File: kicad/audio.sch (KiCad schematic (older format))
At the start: 20 parts

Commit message: ...
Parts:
- added J303: ST-214N, symbol JACK_TRS_6PINS
- gave numbers to parts that had none: 17
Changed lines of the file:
@@
 LIBS:contrib
 LIBS:valves
+LIBS:stm32
 LIBS:ad1955
-LIBS:dcdc
-LIBS:transformer
-LIBS:ir4427
-LIBS:irf9956
-LIBS:usblc6-2
+LIBS:lm4864
 LIBS:synth-cache
 EELAYER 25 0
@@
 $EndDescr
 $Comp
-L JACK_TRS_6PINS J?
+L JACK_TRS_6PINS J301
 U 1 1 5677AE4D
 P 1650 2500
-F 0 "J?" H 1650 2900 50  0000 C CNN
+F 0 "J301" H 1650 2900 50  0000 C CNN
 F 1 "ST-214N" H 1600 2200 50  0000 C CNN
 F 2 "" H 1750 2350 50  0000 C CNN
@@
 $EndComp
 $Comp
-L JACK_TRS_6PINS J?
+L JACK_TRS_6PINS J302
 U 1 1 5677AEE6
 P 1650 4850
-F 0 "J?" H 1650 5250 50  0000 C CNN
+F 0 "J302" H 1650 5250 50  0000 C CNN
 F 1 "ST-214N" H 1600 4550 50  0000 C CNN
 F 2 "" H 1750 4700 50  0000 C CNN
@@
 $EndComp
 $Comp
-L MCP6004 U?
+L MCP6004 U301
 U 1 1 5677B105
 P 3750 1800
-F 0 "U?" H 3800 2000 50  0000 C CNN
+F 0 "U301" H 3800 2000 50  0000 C CNN
 F 1 "AD824" H 3900 1600 50  0000 C CNN
 F 2 "" H 3700 1900 50  0000 C CNN
@@
 $EndComp
 $Comp
-L MCP6004 U?
+L MCP6004 U301
 U 2 1 5677B146
 P 3750 2950
-F 0 "U?" H 3800 3150 50  0000 C CNN
+F 0 "U301" H 3800 3150 50  0000 C CNN
 F 1 "AD824" H 3900 2750 50  0000 C CNN
 F 2 "" H 3700 3050 50  0000 C CNN
@@
 $EndComp
 $Comp
-L MCP6004 U?
+L MCP6004 U301
 U 3 1 5677B1C5
 P 3750 4150
-F 0 "U?" H 3800 4350 50  0000 C CNN
+F 0 "U301" H 3800 4350 50  0000 C CNN
 F 1 "AD824" H 3900 3950 50  0000 C CNN
 F 2 "" H 3700 4250 50  0000 C CNN
@@
 $EndComp
 $Comp
-L MCP6004 U?
+L MCP6004 U301
 U 4 1 5677B248
 P 3750 5350
-F 0 "U?" H 3800 5550 50  0000 C CNN
+F 0 "U301" H 3800 5550 50  0000 C CNN
 F 1 "AD824" H 3900 5150 50  0000 C CNN
 F 2 "" H 3700 5450 50  0000 C CNN
@@
 $EndComp
 $Comp
-L CP1 C?
+L CP1 C301
 U 1 1 5677B391
 P 2700 1900
-F 0 "C?" H 2725 2000 50  0000 L CNN
+F 0 "C301" H 2725 2000 50  0000 L CNN
 F 1 "10.0" H 2725 1800 50  0000 L CNN
 F 2 "" H 2700 1900 50  0000 C CNN
@@
 $EndComp
 $Comp
-L R_Small R?
+L R_Small R301
 U 1 1 5677B458
 P 3150 1900
-F 0 "R?" H 3180 1920 50  0000 L CNN
+F 0 "R301" H 3180 1920 50  0000 L CNN
 F 1 "1K" H 3180 1860 50  0000 L CNN
 F 2 "" H 3150 1900 50  0000 C CNN
@@
 	2350 1900 2550 1900
 $Comp
-L R_Small R?
+L R_Small R308
 U 1 1 5677B594
 P 3850 1200
-F 0 "R?" H 3900 1250 50  0000 L CNN
+F 0 "R308" H 3900 1250 50  0000 L CNN
 F 1 "100K" H 3900 1150 50  0000 L CNN
 F 2 "" H 3850 1200 50  0000 C CNN
@@
 Connection ~ 4050 1800
 $Comp
-L GNDA #PWR?
+L GNDA #PWR046
 U 1 1 5677B8F7
 P 3650 2100
-F 0 "#PWR?" H 3650 1850 50  0001 C CNN
+F 0 "#PWR046" H 3650 1850 50  0001 C CNN
 F 1 "GNDA" H 3650 1950 39  0000 C CNN
 F 2 "" H 3650 2100 50  0000 C CNN
@@
 $EndComp
 Wire Wire Line
-	3650 900  3650 1000
-Wire Wire Line
-	3650 1000 3650 1500
+	3650 900  3650 1500
 Text Label 3650 900  0    60   ~ 0
 +3V3A_CPU
 $Comp
-L CP1 C?
+L CP1 C302
 U 1 1 5677BFEC
 P 2700 3050
-F 0 "C?" H 2725 3150 50  0000 L CNN
+F 0 "C302" H 2725 3150 50  0000 L CNN
 F 1 "10.0" H 2725 2950 50  0000 L CNN
 F 2 "" H 2700 3050 50  0000 C CNN
@@
 $EndComp
 $Comp
-L R_Small R?
+L R_Small R302
 U 1 1 5677BFF2
 P 3150 3050
-F 0 "R?" H 3180 3070 50  0000 L CNN
+F 0 "R302" H 3180 3070 50  0000 L CNN
 F 1 "1K" H 3180 3010 50  0000 L CNN
 F 2 "" H 3150 3050 50  0000 C CNN
@@
 	2350 3050 2550 3050
 $Comp
-L R_Small R?
+L R_Small R305
 U 1 1 5677BFFB
 P 3800 2550
-F 0 "R?" H 3850 2600 50  0000 L CNN
+F 0 "R305" H 3850 2600 50  0000 L CNN
 F 1 "100K" H 3850 2500 50  0000 L CNN
 F 2 "" H 3800 2550 50  0000 C CNN
@@
 Connection ~ 4050 2950
 $Comp
-L GNDA #PWR?
+L GNDA #PWR047
 U 1 1 5677C008
 P 3650 3250
-F 0 "#PWR?" H 3650 3000 50  0001 C CNN
+F 0 "#PWR047" H 3650 3000 50  0001 C CNN
 F 1 "GNDA" H 3650 3100 39  0000 C CNN
 F 2 "" H 3650 3250 50  0000 C CNN
@@
 $EndComp
 $Comp
-L CP1 C?
+L CP1 C303
 U 1 1 5677C595
 P 2700 4250
-F 0 "C?" H 2725 4350 50  0000 L CNN
+F 0 "C303" H 2725 4350 50  0000 L CNN
 F 1 "10.0" H 2725 4150 50  0000 L CNN
 F 2 "" H 2700 4250 50  0000 C CNN
@@
 $EndComp
 $Comp
-L R_Small R?
+L R_Small R303
 U 1 1 5677C59B
 P 3150 4250
-F 0 "R?" H 3180 4270 50  0000 L CNN
+F 0 "R303" H 3180 4270 50  0000 L CNN
 F 1 "1K" H 3180 4210 50  0000 L CNN
 F 2 "" H 3150 4250 50  0000 C CNN
@@
 	2550 4250 2400 4250
 $Comp
-L R_Small R?
+L R_Small R306
 U 1 1 5677C5A4
 P 3800 3750
-F 0 "R?" H 3850 3800 50  0000 L CNN
+F 0 "R306" H 3850 3800 50  0000 L CNN
 F 1 "100K" H 3850 3700 50  0000 L CNN
 F 2 "" H 3800 3750 50  0000 C CNN
@@
 Connection ~ 4050 4150
 $Comp
-L GNDA #PWR?
+L GNDA #PWR048
 U 1 1 5677C5B1
 P 3650 4450
-F 0 "#PWR?" H 3650 4200 50  0001 C CNN
+F 0 "#PWR048" H 3650 4200 50  0001 C CNN
 F 1 "GNDA" H 3650 4300 39  0000 C CNN
 F 2 "" H 3650 4450 50  0000 C CNN
@@
 $EndComp
 $Comp
-L CP1 C?
+L CP1 C304
 U 1 1 5677C832
 P 2700 5450
-F 0 "C?" H 2725 5550 50  0000 L CNN
+F 0 "C304" H 2725 5550 50  0000 L CNN
 F 1 "10.0" H 2725 5350 50  0000 L CNN
 F 2 "" H 2700 5450 50  0000 C CNN
@@
 $EndComp
 $Comp
-L R_Small R?
+L R_Small R304
 U 1 1 5677C838
 P 3150 5450
-F 0 "R?" H 3180 5470 50  0000 L CNN
+F 0 "R304" H 3180 5470 50  0000 L CNN
 F 1 "1K" H 3180 5410 50  0000 L CNN
 F 2 "" H 3150 5450 50  0000 C CNN
@@
 	2550 5450 2400 5450
 $Comp
-L R_Small R?
+L R_Small R307
 U 1 1 5677C841
 P 3800 4950
-F 0 "R?" H 3850 5000 50  0000 L CNN
+F 0 "R307" H 3850 5000 50  0000 L CNN
 F 1 "100K" H 3850 4900 50  0000 L CNN
 F 2 "" H 3800 4950 50  0000 C CNN
@@
 Connection ~ 4050 5350
 $Comp
-L GNDA #PWR?
+L GNDA #PWR049
 U 1 1 5677C84E
 P 3650 5650
-F 0 "#PWR?" H 3650 5400 50  0001 C CNN
+F 0 "#PWR049" H 3650 5400 50  0001 C CNN
 F 1 "GNDA" H 3650 5500 39  0000 C CNN
 F 2 "" H 3650 5650 50  0000 C CNN
@@
 $EndComp
 $Comp
-L CP1 C?
+L CP1 C305
 U 1 1 5677D086
 P 4750 1250
-F 0 "C?" H 4775 1350 50  0000 L CNN
+F 0 "C305" H 4775 1350 50  0000 L CNN
 F 1 "10.0" H 4775 1150 50  0000 L CNN
 F 2 "" H 4750 1250 50  0000 C CNN
@@
 $EndComp
 $Comp
-L C_Small C?
+L C_Small C306
 U 1 1 5677D24B
 P 5050 1250
-F 0 "C?" H 5060 1320 50  0000 L CNN
+F 0 "C306" H 5060 1320 50  0000 L CNN
 F 1 "C_Small" H 5060 1170 50  0000 L CNN
 F 2 "" H 5050 1250 50  0000 C CNN
@@
 $EndComp
 Wire Wire Line
-	4750 1100 4900 1100
-Wire Wire Line
-	4900 1100 5050 1100
+	4750 1100 5050 1100
 Wire Wire Line
 	5050 1100 5050 1150
 Wire Wire Line
-	4750 1400 4900 1400
-Wire Wire Line
-	4900 1400 5050 1400
+	4750 1400 5050 1400
 Wire Wire Line
 	5050 1400 5050 1350
@@
 Connection ~ 4900 1400
 $Comp
-L GNDA #PWR?
+L GNDA #PWR050
 U 1 1 5677D37F
 P 4900 1450
-F 0 "#PWR?" H 4900 1200 50  0001 C CNN
+F 0 "#PWR050" H 4900 1200 50  0001 C CNN
 F 1 "GNDA" H 4900 1300 39  0000 C CNN
 F 2 "" H 4900 1450 50  0000 C CNN
@@
 	2050 2300 2200 2300
 $Comp
-L GNDA #PWR?
+L GNDA #PWR051
 U 1 1 5677DCC4
 P 2200 2300
-F 0 "#PWR?" H 2200 2050 50  0001 C CNN
+F 0 "#PWR051" H 2200 2050 50  0001 C CNN
 F 1 "GNDA" H 2200 2150 39  0000 C CNN
 F 2 "" H 2200 2300 50  0000 C CNN
@@
 	2050 4650 2250 4650
 $Comp
-L GNDA #PWR?
+L GNDA #PWR052
 U 1 1 5677F43E
 P 2250 4650
-F 0 "#PWR?" H 2250 4400 50  0001 C CNN
+F 0 "#PWR052" H 2250 4400 50  0001 C CNN
 F 1 "GNDA" H 2250 4500 39  0000 C CNN
 F 2 "" H 2250 4650 50  0000 C CNN
@@
 Text Notes 1650 3750 0    60   ~ 0
 http://3.bp.blogspot.com/-bP_h_C9MMF0/UXzus0086cI/AAAAAAAACZU/TzdCaGjU_u4/s1600/Op-Amp+audio+mixer+Circuit.gif
+$Comp
+L JACK_TRS_6PINS J303
+U 1 1 56838775
+P 1650 6500
+F 0 "J303" H 1650 6900 50  0000 C CNN
+F 1 "ST-214N" H 1600 6200 50  0000 C CNN
+F 2 "" H 1750 6350 50  0000 C CNN
+F 3 "" H 1750 6350 50  0000 C CNN
+	1    1650 6500
+	1    0    0    -1
+$EndComp
 $EndSCHEMATC

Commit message: ...
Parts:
- removed C302: 10.0, symbol CP1
- removed J303: ST-214N, symbol JACK_TRS_6PINS
- removed R302, R303, R304: 1K, symbol R_Small
- removed R305, R306, R307: 100K, symbol R_Small
- added C? (x4): 82, symbol C_Small
- added C? (x2): 4700, symbol C_Small
- added C?: 0.01, symbol C_Small
- added C?: 10.0, symbol CP1
- added C? (x2): 470, symbol C_Small
- added J?: ST-214N, symbol JACK_TRS_6PINS
- added R? (x3): 3K3, symbol R_Small
- added R? (x2): 47K, symbol R_Small
- added R?: 100K, symbol R_Small
- added R? (x2): 10K, symbol R_Small
- added R? (x2): 20K, symbol R_Small
- added R? (x2): 6K8, symbol R_Small
- C306: value C_Small -> 0.01
- R301: value 1K -> 3K3
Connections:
- net +3V3A_CPU: now also R?.2
- net GNDA: now also C?.1, C?.1, C?.1, C?.1, C?.2, J?.1 (S), R?.1; no longer U301.11 (V-), U301.11 (V-), U301.11 (V-)
- net at C301.1, J301.2 (T): now also J301.3 (R)
- net at U301.2 (-): now also C?.1, R?.1; no longer R301.1
- net at R308.2: now also R301.1, C?.2, R?.2; no longer U301.3 (+)
- net Vb: now reaches U301.5 (+)
- net Vb: now also U301.10 (+), U301.12 (+), U301.3 (+), C?.1, R?.1, R?.2
- net at U301.6 (-): now also C?.1, R?.1
- net at U301.9 (-): now also C?.1, R?.1
- net at U301.13 (-): now also C?.1, R?.1
- net at C303.2: now also R?.2
- net at C304.2: now also R?.2
- net AUDIO1_L renamed HIGAIN1
- net HIGAIN1: now also C?.2
- net AUDIO1_R renamed HIGAIN2
- net HIGAIN2: now also C?.2, R?.1
- net AUDIO2_L renamed LINEIN_L
- net LINEIN_L: now also C?.2, R?.1
- net AUDIO2_R renamed LINEIN_R
- net LINEIN_R: now also C?.2, R?.1
- new net: C?.1, J?.2 (T), J?.3 (R)
- new net: C?.2, R?.2
- new net: C?.2, R?.1, R?.2, R?.2 (x3)
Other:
- note removed: "Investigate input impedance!"
- note removed: "This symbol is incorrect!"
- note removed: "http://3.bp.blogspot.com/-bP_h_C9MMF0/UXzus0086cI/AAAAAAAACZU/TzdCaGjU_u4/s1600/Op-Amp+audio+mixer+Circuit.gif"
- note removed: "implement 1st order lowpass filters here"
- moved on the sheet: C301, C303, C304, J301, J302, R301, R308, U301B, U301C, U301D

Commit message: ...
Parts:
- added C? (x2): 1.0, symbol C_Small
- added D? (x4): BAT54S, symbol D_Schottky_x2_Serial_AKC
- added D? (x3): LED, symbol LED
- added R? (x3): 10K, symbol R_Small
- added R? (x3): 220, symbol R_Small
- added RV? (x2): PTD901-2015K-B103 10K, symbol POT
- C301, C303, C304, C?: value 10.0 -> 22.0
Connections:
- net +3V3A_CPU: now also D?.2 (K), D?.2 (K), D?.2 (K), D?.2 (K), R?.2, R?.2, R?.2, RV?.3, RV?.3
- net GNDA: now also C?.2, C?.2, D?.1 (A), D?.1 (A), D?.1 (A), D?.1 (A), D?.1 (K), D?.1 (K), D?.1 (K), RV?.1, RV?.1
- net PLUG_1: now reaches J301.4 (SN)
- net PLUG_1: now also R?.1
- net PLUG_3: now reaches J302.4 (SN)
- net PLUG_3: now also R?.1
- net at C?.2, R301.1, R308.2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: now also D?.3 (common)
- net at C?.2, R?.1, R?.2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: now also D?.3 (common) (x3)
- net PLUG_2: now reaches J?.4 (SN)
- net PLUG_2: now also R?.1
- new net: D?.2 (A), R?.1 (x3)
- new net LEDPLUG1: R?.2
- new net LEDPLUG2: R?.2
- new net LEDPLUG3: R?.2
- new net POT1: C?.1, RV?.2
- new net POT2: C?.1, RV?.2
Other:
- moved on the sheet: C301, C303, C304, C305, C306, C?, J301, J302, J?, R301, R308, R?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

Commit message: ...
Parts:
- removed J301, J302, J?: ST-214N, symbol JACK_TRS_6PINS
- removed R? (x3): 10K, symbol R_Small
- added J401, J402, J403: KATE_3.5MM_6, jacks:JACK_35MM_KATE_6, symbol KATE_3.5MM_6
- added R404: 47K, Resistors_SMD:R_0805, symbol R
- added R405, R406: 47K, Resistors_SMD:R_0805, symbol R_Small
- C401: renamed from C?; footprint (none) -> Capacitors_Tantalum_SMD:TantalC_SizeC_EIA-6032_Reflow
- C402: renamed from C301; footprint (none) -> Capacitors_Tantalum_SMD:TantalC_SizeC_EIA-6032_Reflow
- C403: renamed from C303; footprint (none) -> Capacitors_Tantalum_SMD:TantalC_SizeC_EIA-6032_Reflow
- C404: renamed from C304; footprint (none) -> Capacitors_Tantalum_SMD:TantalC_SizeC_EIA-6032_Reflow
- C405, C406, C407, C408, C409, C410, C411, C412, C415, C416, C417: renamed from C?; footprint (none) -> Capacitors_SMD:C_0805
- C413: renamed from C305; footprint (none) -> Capacitors_SMD:C_0805
- C414: renamed from C306; footprint (none) -> Capacitors_SMD:C_0805
- D401, D402, D403: renamed from D?; footprint (none) -> LEDs:LED-0805
- D404, D405, D406, D407: renamed from D?; footprint (none) -> TO_SOT_Packages_SMD:SOT-23
- R401, R402, R403, R407, R409, R410, R411, R412, R413, R414, R416, R417, R418, R419, R420: renamed from R?; footprint (none) -> Resistors_SMD:R_0805
- R408: renamed from R301; footprint (none) -> Resistors_SMD:R_0805
- R415: renamed from R308; footprint (none) -> Resistors_SMD:R_0805
- RV401, RV402: renamed from RV?; footprint (none) -> Potentiometers:Potentiometer_Alps-RK16-single_largePads
- U401: renamed from U301; footprint (none) -> Housings_SOIC:SOIC-14_3.9x8.7mm_Pitch1.27mm
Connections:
- net +3V3A_CPU: now also R404.1, R405.2, R406.2
- net GNDA: now also J401.2 (S2), J401.3, J402.2 (S2), J402.3, J403.2 (S2), J403.3
- net PLUG_1: now also J402.1 (S1), J402.4 (S3), R404.2
- net PLUG_2: now also J403.1 (S1), J403.4 (S3), R405.1
- net PLUG_3: now also J401.1 (S1), J401.4 (S3), R406.1
- net at C402.1: now also J402.5 (R), J402.6 (T)
- net at C403.1: now also J401.6 (T)
- net at C404.1: now also J401.5 (R)
- net at C401.1: now also J403.5 (R), J403.6 (T)

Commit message: before moving headphone amp to the left
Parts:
- added Q401, Q402, Q403: Si2301DS, TO_SOT_Packages_SMD:SOT-23, symbol Q_PMOS_GSD
- added R421, R422, R423: 10K, Resistors_SMD:R_0805, symbol R
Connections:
- net +3V3A_CPU: now also Q401.3 (D), Q402.3 (D), Q403.3 (D), R421.2, R422.2, R423.2
- net PLUG_1: now also Q402.1 (G), R422.1
- net PLUG_2: now also Q403.1 (G), R423.1
- net PLUG_3: now also Q401.1 (G), R421.1
- net LEDPLUG1: no longer names the net of R401.2
- net LEDPLUG1: now also Q402.2 (S)
- net LEDPLUG2: no longer names the net of R402.2
- net LEDPLUG2: now also Q403.2 (S)
- net LEDPLUG3: no longer names the net of R403.2
- net LEDPLUG3: now also Q401.2 (S)
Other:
- moved on the sheet: D401, D402, D403, R401, R402, R403

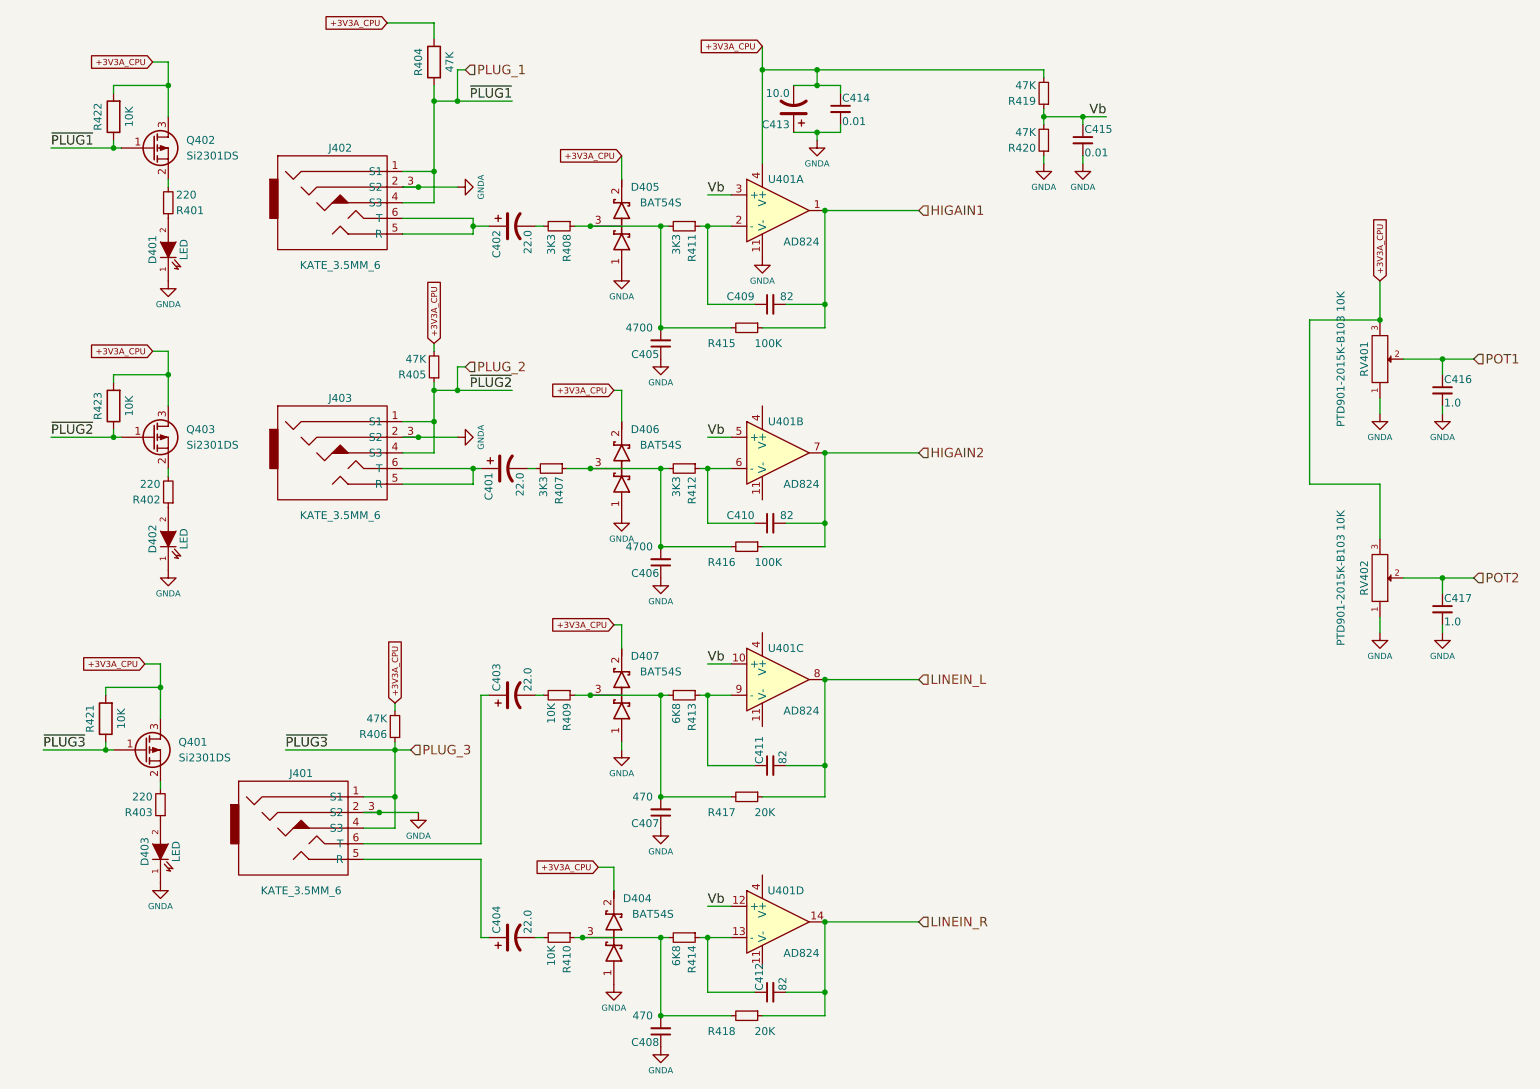
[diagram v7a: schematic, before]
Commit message: fixed p-mosfets
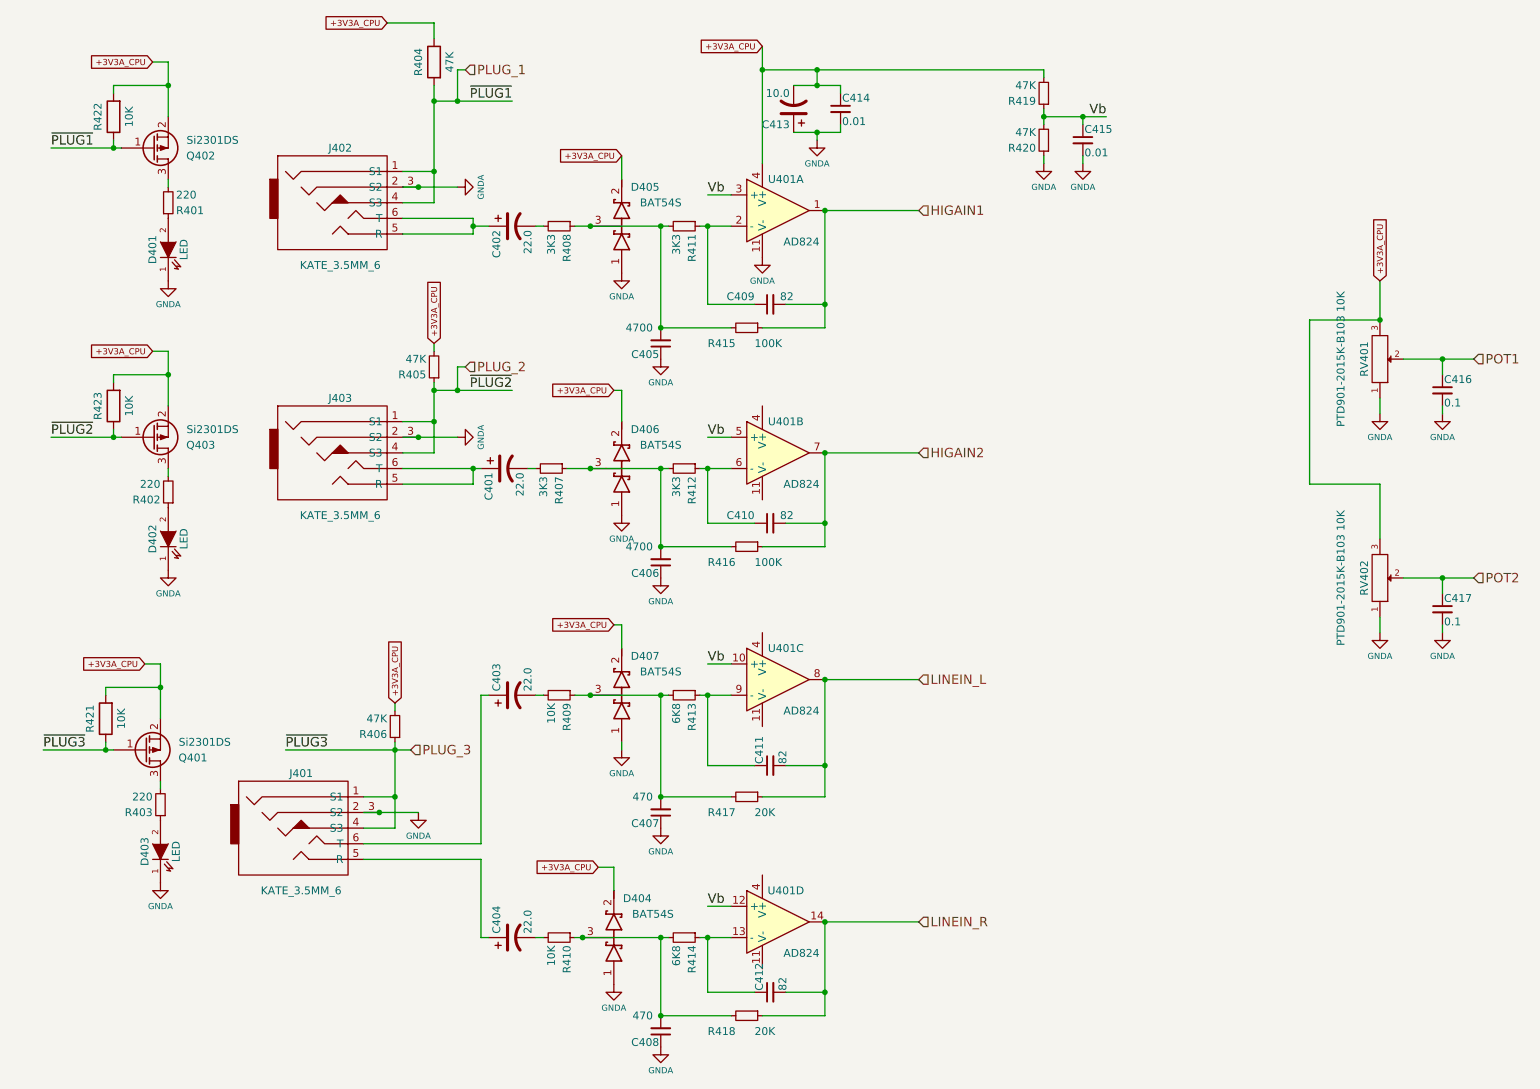
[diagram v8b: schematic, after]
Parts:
- C416, C417: value 1.0 -> 0.1
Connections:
- net +3V3A_CPU: now also Q401.2 (S), Q402.2 (S), Q403.2 (S); no longer Q401.3 (D), Q402.3 (D), Q403.3 (D)
- net at R401.2: now also Q402.3 (D); no longer Q402.2 (S)
- net at R402.2: now also Q403.3 (D); no longer Q403.2 (S)
- net at R403.2: now also Q401.3 (D); no longer Q401.2 (S)
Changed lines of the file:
@@
 P 9550 2950
 F 0 "C416" H 9560 3020 50  0000 L CNN
-F 1 "1.0" H 9560 2870 50  0000 L CNN
+F 1 "0.1" H 9560 2870 50  0000 L CNN
 F 2 "Capacitors_SMD:C_0805" H 9550 2950 50  0001 C CNN
 F 3 "" H 9550 2950 50  0000 C CNN
@@
 P 9550 4350
 F 0 "C417" H 9560 4420 50  0000 L CNN
-F 1 "1.0" H 9560 4270 50  0000 L CNN
+F 1 "0.1" H 9560 4270 50  0000 L CNN
 F 2 "Capacitors_SMD:C_0805" H 9550 4350 50  0001 C CNN
 F 3 "" H 9550 4350 50  0000 C CNN
@@
 F 3 "" H 1300 1400 50  0000 C CNN
 	1    1300 1400
-	1    0    0    -1
+	1    0    0    1
 $EndComp
 Text GLabel 1300 850  0    39   Input ~ 0
@@
 F 3 "" H 1300 3250 50  0000 C CNN
 	1    1300 3250
-	1    0    0    -1
+	1    0    0    1
 $EndComp
 Text GLabel 1300 2700 0    39   Input ~ 0
@@
 F 3 "" H 1250 5250 50  0000 C CNN
 	1    1250 5250
-	1    0    0    -1
+	1    0    0    1
 $EndComp
 Text GLabel 1250 4700 0    39   Input ~ 0
